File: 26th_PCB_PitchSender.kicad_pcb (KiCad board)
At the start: 2 copper layers, 120 x 28.4 mm, 21 parts, among them J1 vol, J2 Conn_01x04_Pin, J3 microSD, J4 Conn_01x04_Socket, J5 BNO055, J6 BMP390

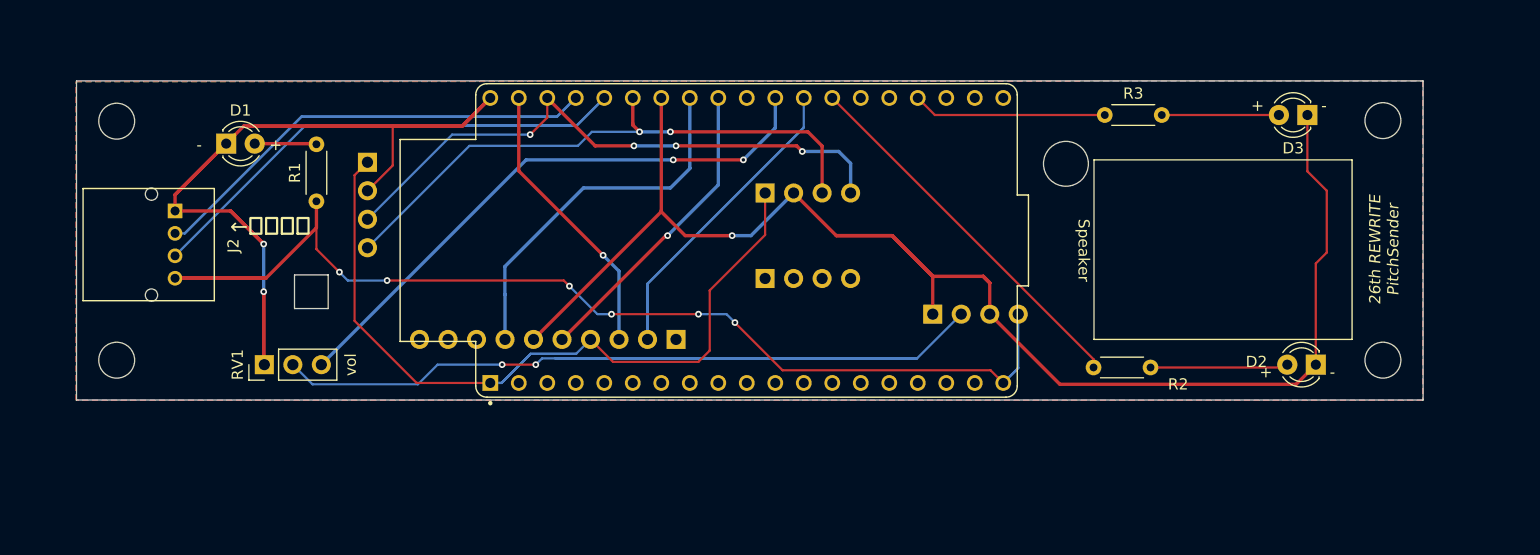
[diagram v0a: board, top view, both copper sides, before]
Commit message: Add status LED
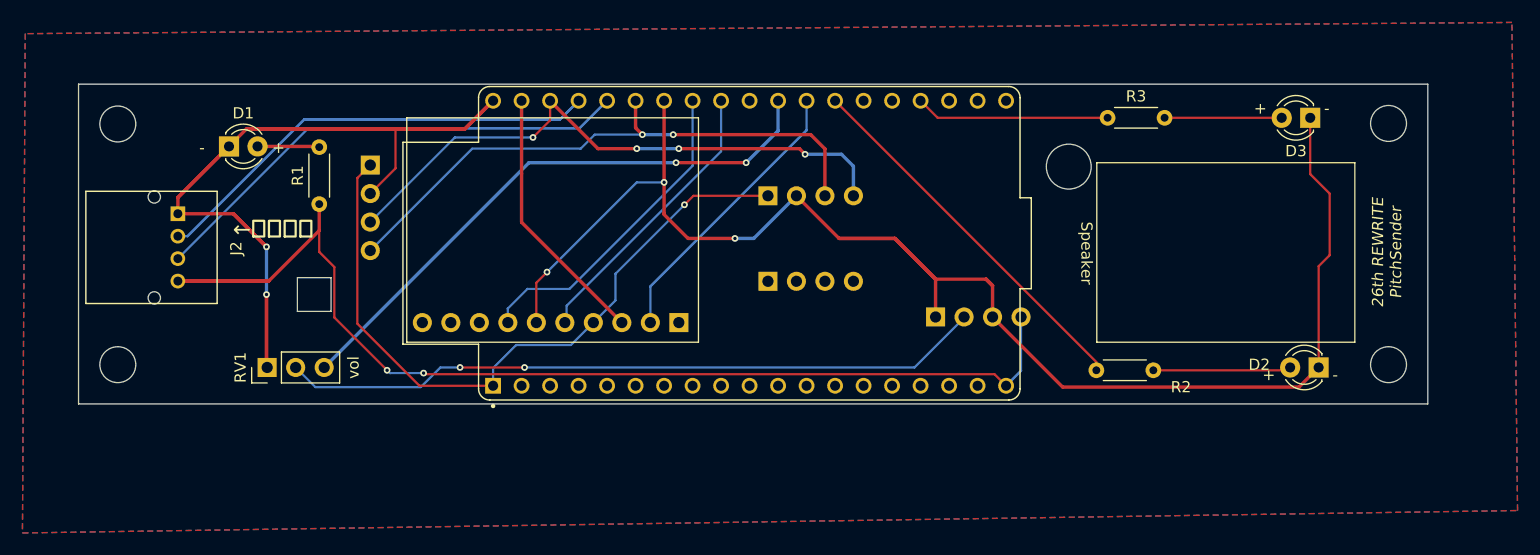
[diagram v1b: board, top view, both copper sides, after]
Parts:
- moved J3 1.52 mm to (155.0, 97.8)
- moved H2 0.64 mm to (218.2, 101.5)
- moved H1 0.56 mm to (218.2, 80.0)
- moved H4 0.41 mm to (105.0, 101.5)
- moved D1 0.35 mm to (114.9, 82.0)
- moved H5 0.35 mm to (189.8, 83.8)
- moved J1 0.35 mm to (177.9, 97.2)
- moved J2 0.35 mm to (110.4, 91.0)
- moved J4 0.35 mm to (162.9, 86.5)
- moved J5 0.35 mm to (162.9, 94.1)
- moved JLCPCB_LOGO 0.35 mm to (128.2, 79.0)
- moved REWRITE_LOGO 0.35 mm to (206.4, 90.4)
- moved U1 0.35 mm to (161.3, 90.7)
- moved J6 0.35 mm to (127.5, 83.7)
- moved R1 0.35 mm to (123.0, 87.2)
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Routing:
- net Net-(J1-Pin_2): track 95.1 -> 62.9 mm
- net +3V3: track 76.2 -> 62.8 mm, vias 0 -> 1
- net /ChipSelect: track 51.9 -> 45.2 mm
- net /MISO: track 32.9 -> 28.8 mm
- net +5V: track 109.7 -> 112.3 mm, vias 6 -> 2
- net GND: track 243.4 -> 246.0 mm, vias 3 -> 5
- net /SCK: track 27.4 -> 25.5 mm, vias 1 -> 0
- net /MOSI: track 25.2 -> 23.4 mm, vias 1 -> 0
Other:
- board size 120 x 28.4 mm -> 120.2 x 28.5 mm
- board text added: "3V3"

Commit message: ESP32とスピーカー場所交代
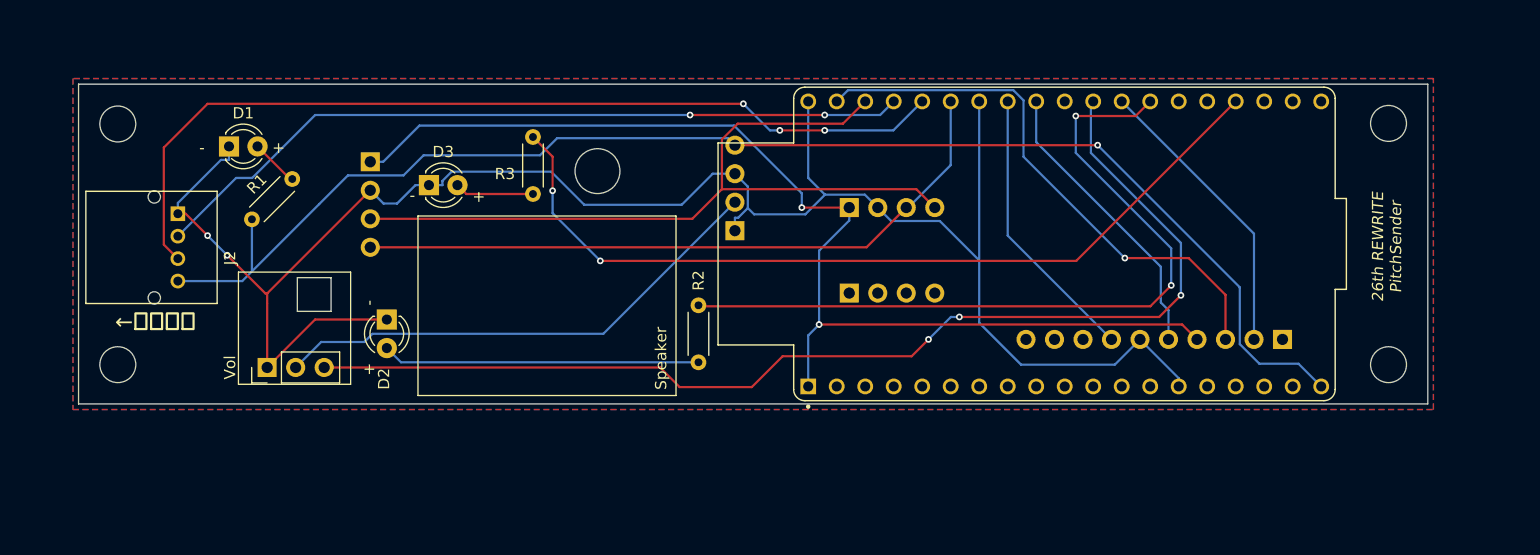
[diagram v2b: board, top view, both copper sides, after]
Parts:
- removed the REWRITE_LOGO at (206.4, 90.4)
- added REWRITE_LOGO: LOGO, lib:REWRITE_LOGO, B.Cu at (143.2, 96.2)
- J1: value vol -> Amp
- J4: value Conn_01x04_Socket -> BNO055
- RV1: value vol -> Vol
- moved D2 83.2 mm to (129.0, 97.5), turned to -90 degrees
- moved D3 78.8 mm to (132.7, 85.5), turned to 0 degrees
- moved J3 53.8 mm to (208.8, 99.2)
- moved R3 51.2 mm to (142.0, 81.2), turned to -90 degrees
- moved H5 42.0 mm to (147.8, 84.2)
- moved R2 35.9 mm to (156.8, 96.2), turned to -90 degrees
- moved U1 28.1 mm to (189.4, 90.7)
- moved J1 19.5 mm to (160.0, 89.6), turned to 0 degrees
- moved J5 7.32 mm to (170.2, 95.1)
- moved J4 7.32 mm to (170.2, 87.5)
- moved R1 6.15 mm to (117.0, 88.5), turned to 45 degrees
- moved JLCPCB_LOGO 3.36 mm to (131.5, 79.2)
- moved J6 0.29 mm to (127.5, 83.4)
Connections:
- U1 pad J2_14: unconnected-(U1-GND_J2_14-PadJ2_14) -> GND
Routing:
- net GND: track 246.0 -> 169.4 mm, vias 5 -> 2
- net Net-(U1-IO15): track 17.3 -> 76.0 mm, vias 0 -> 2
- net /SPK: track 51.9 -> 101.2 mm, vias 2 -> 3
- net +3V3: track 62.8 -> 99.5 mm, vias 1 -> 2
- net Net-(U1-IO4): track 33.7 -> 68.7 mm, vias 0 -> 2
- net /MOSI: track 23.4 -> 49.5 mm, vias 0 -> 1
- net /ChipSelect: track 45.2 -> 26.1 mm
- net Net-(J1-Pin_2): track 62.9 -> 45.3 mm, vias 2 -> 0
- net /SCL: track 53.6 -> 70.7 mm, vias 4 -> 0
- net Net-(D2-A): track 12.3 -> 28.3 mm
- net /BicoRX-psdTX: track 80.6 -> 68.8 mm, vias 0 -> 2
- net +5V: track 112.3 -> 123.9 mm, vias 2 -> 1
- net /BicoTX-psdRX: track 71.7 -> 81.7 mm, vias 0 -> 3
- net /SDA: track 52.8 -> 60.4 mm, vias 2 -> 0
- net /MISO: track 28.8 -> 25.0 mm
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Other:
- board text added: "<-RX"
- board text added: "IN+"
- board text added: "IN-"
- board text added: "TX->"
- board text added: "V+"
- board text removed: "<-TX"
- board text removed: "RX->"
